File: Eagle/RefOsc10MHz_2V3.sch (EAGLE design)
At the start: 72 parts, among them CON1 TYCO-AMP_USBUSB-B_SMT, CON2 HEADER-2X5, CON3 SD-73100-0105, CON5 AVR-JTAG-10, CON6 HEADER-2X3, CON7 MCX-J-P-X-RA-SM1, U1 ATmega328-P, U2 LC4032V_XXT44, U3 74HCT221D, U5 OPA354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

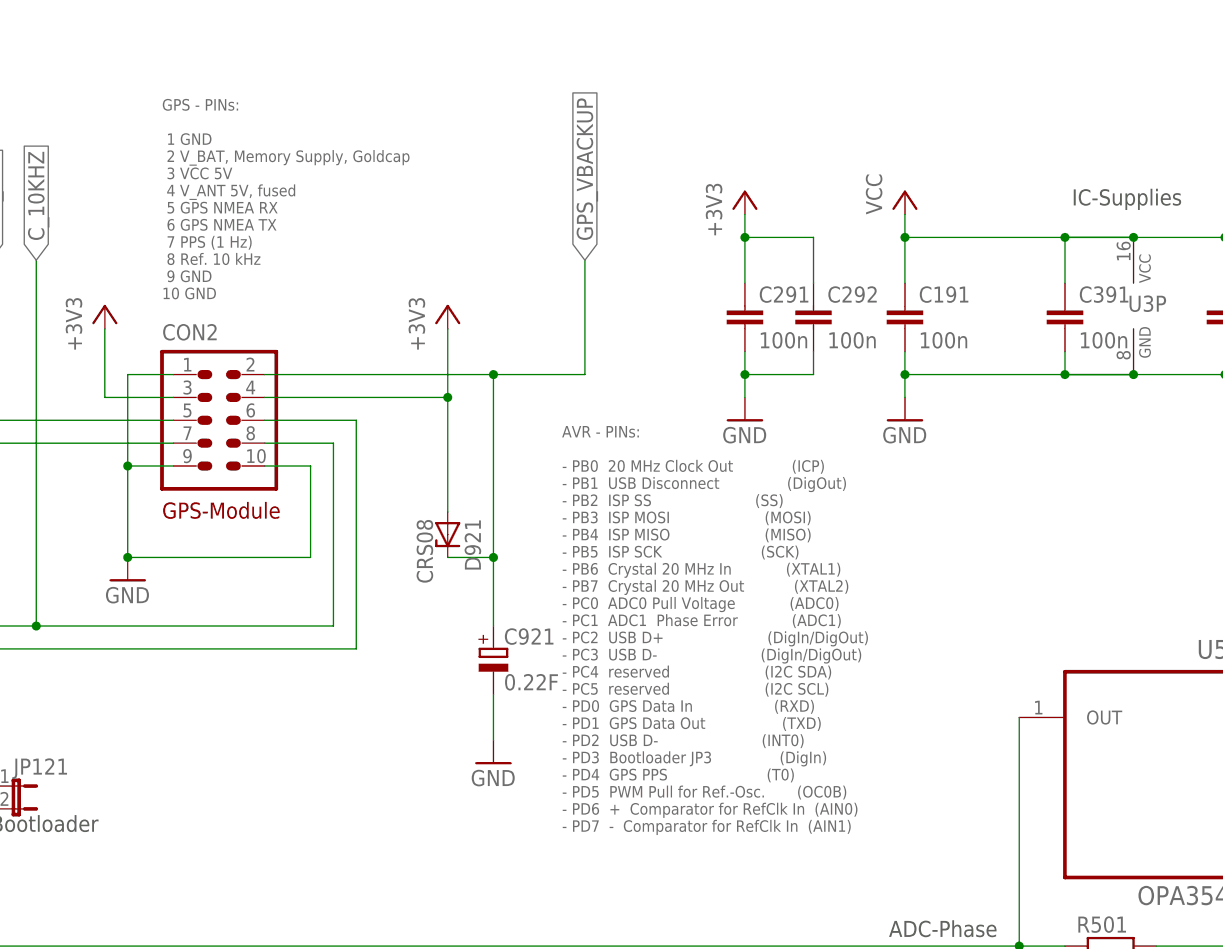
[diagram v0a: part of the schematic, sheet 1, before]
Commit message: HW_V2.3.1 - GPS connector - fixed 5V to 3V3 in info block
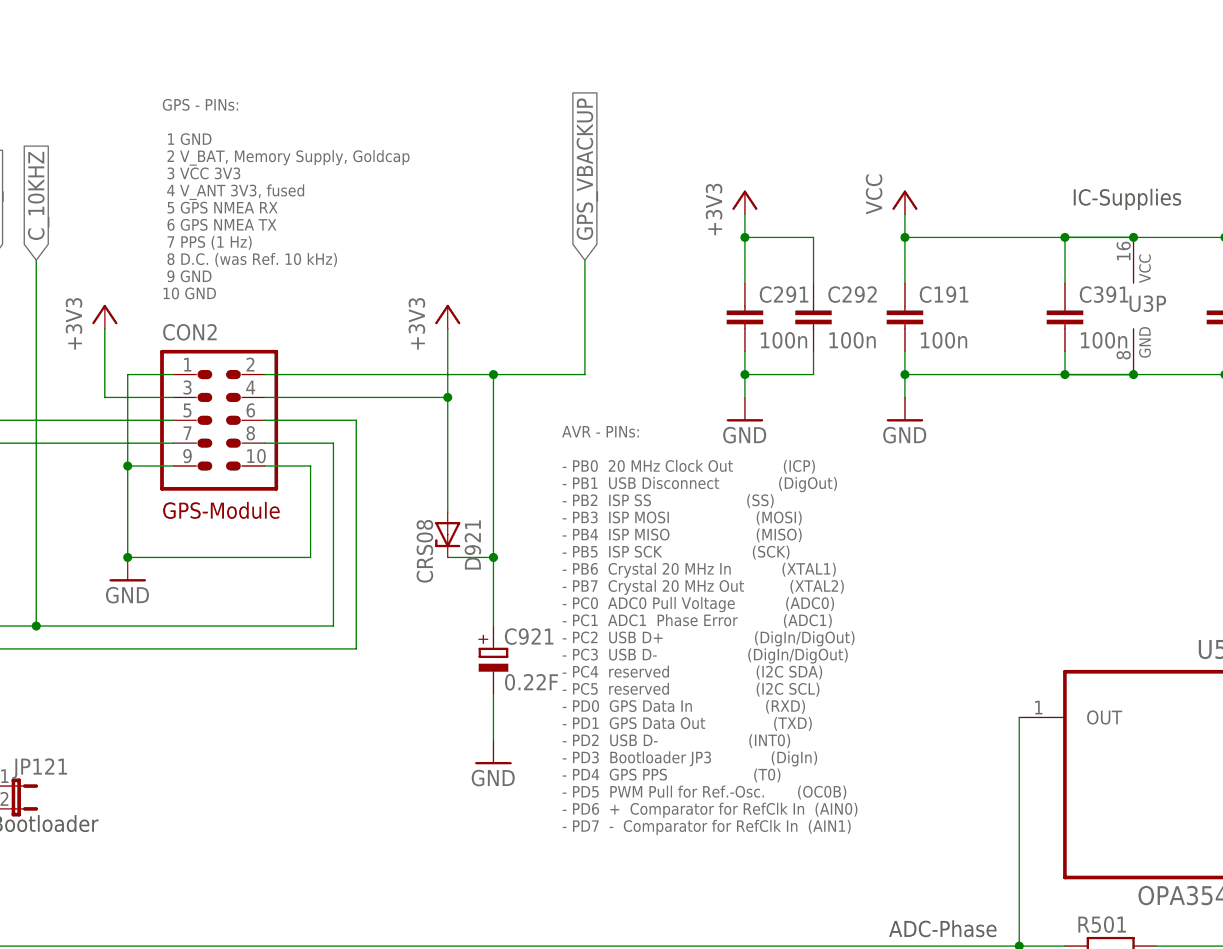
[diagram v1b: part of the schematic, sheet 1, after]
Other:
- note added: "GPS - PINs: 1 GND 2 V_BAT, Memory Supply, Goldcap 3 VCC 3V3 4 V_ANT 3V3, fused 5 GPS NMEA RX 6 GPS NMEA TX 7 PPS (1 Hz) 8 D.C. (was Ref. 10 kHz) 9 GND 10 GND"
- note removed: "GPS - PINs: 1 GND 2 V_BAT, Memory Supply, Goldcap 3 VCC 5V 4 V_ANT 5V, fused 5 GPS NMEA RX 6 GPS NMEA TX 7 PPS (1 Hz) 8 Ref. 10 kHz 9 GND 10 GND"
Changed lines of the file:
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@@
 <text x="10.414" y="115.062" size="1.778" layer="94">USB-B</text>
 <text x="243.84" y="203.2" size="1.27" layer="96" font="fixed">AVR - PINs:
-- PB0  20 MHz Clock Out             (ICP)
-- PB1  USB Disconnect               (DigOut)
-- PB2  ISP SS                       (SS)
-- PB3  ISP MOSI                     (MOSI)
-- PB4  ISP MISO                     (MISO)
-- PB5  ISP SCK                      (SCK)
-- PB6  Crystal 20 MHz In            (XTAL1)
-- PB7  Crystal 20 MHz Out           (XTAL2)
-- PC0  ADC0 Pull Voltage            (ADC0)
-- PC1  ADC1  Phase Error            (ADC1)
-- PC2  USB D+                       (DigIn/DigOut)
-- PC3  USB D-                       (DigIn/DigOut)
-- PC4  reserved                     (I2C SDA)
-- PC5  reserved                     (I2C SCL)
-- PD0  GPS Data In                  (RXD)
-- PD1  GPS Data Out                 (TXD)
-- PD2  USB D-                       (INT0)
-- PD3  Bootloader JP3               (DigIn)
-- PD4  GPS PPS                      (T0)
+- PB0  20 MHz Clock Out           (ICP)
+- PB1  USB Disconnect             (DigOut)
+- PB2  ISP SS                     (SS)
+- PB3  ISP MOSI                   (MOSI)
+- PB4  ISP MISO                   (MISO)
+- PB5  ISP SCK                    (SCK)
+- PB6  Crystal 20 MHz In           (XTAL1)
+- PB7  Crystal 20 MHz Out          (XTAL2)
+- PC0  ADC0 Pull Voltage           (ADC0)
+- PC1  ADC1  Phase Error          (ADC1)
+- PC2  USB D+                    (DigIn/DigOut)
+- PC3  USB D-                    (DigIn/DigOut)
+- PC4  reserved                   (I2C SDA)
+- PC5  reserved                   (I2C SCL)
+- PD0  GPS Data In                (RXD)
+- PD1  GPS Data Out               (TXD)
+- PD2  USB D-                    (INT0)
+- PD3  Bootloader JP3             (DigIn)
+- PD4  GPS PPS                   (T0)
 - PD5  PWM Pull for Ref.-Osc.       (OC0B)
 - PD6  +  Comparator for RefClk In  (AIN0)
@@
  1 GND
  2 V_BAT, Memory Supply, Goldcap
- 3 VCC 5V
- 4 V_ANT 5V, fused
+ 3 VCC 3V3
+ 4 V_ANT 3V3, fused
  5 GPS NMEA RX
  6 GPS NMEA TX
  7 PPS (1 Hz)
- 8 Ref. 10 kHz
+ 8 D.C. (was Ref. 10 kHz)
  9 GND
 10 GND</text>
